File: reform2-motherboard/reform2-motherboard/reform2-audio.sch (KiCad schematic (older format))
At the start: 36 parts, among them J21 Conn_01x04_Male, J7 SJ-43516-SMT, U20 WM8731, U21 MAX9715ETE+

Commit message: reform2: first motherboard fully routed, checks TBD
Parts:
- added J16: LINE_IN, Connector_PinHeader_2.54mm:PinHeader_1x03_P2.54mm_Vertical, symbol Connector:Conn_01x03_Male
- added R112, R66: 220, Resistor_SMD:R_0603_1608Metric, symbol Device:R_Small
- added R114, R121, R150, R151: 33, Resistor_SMD:R_0603_1608Metric, symbol Device:R_Small
- added R152: 0, Resistor_SMD:R_0603_1608Metric, symbol Device:R_Small
- added TP1: T_GAIN, TestPoint:TestPoint_Pad_1.0x1.0mm, symbol Connector:TestPoint
- J21: footprint Connector_PinSocket_2.54mm:PinSocket_1x04_P2.54mm_Vertical -> Connector_PinHeader_2.54mm:PinHeader_1x04_P2.54mm_Vertical
- R138: value 0 -> 33
- R139: value 100 -> 33; Manufacturer Vishay Dale -> (none); Manufacturer_No CRCW0603100RFKEAC -> (none)
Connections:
- net +5V: now also R152.2
- net DAC_BCLK: now also R114.1; no longer U20.3 (BCLK)
- net DAC_DIN: now also R150.1; no longer U20.6 (ADCDAT)
- net DAC_DOUT: now also R121.1; no longer U20.4 (DACDAT)
- net DAC_RXFS: now also R139.1; no longer U20.7 (ADCLRC)
- net DAC_SCL: now also R66.1; no longer R135.2, U20.24 (SCLK)
- net DAC_SDA: now also R112.1; no longer R136.2, U20.23 (SDIN)
- net DAC_TXFS: now also R151.1; no longer U20.5 (DACLRC)
- net GND: now also J16.1 (Pin_1)
- net at U20.19 (RLINEIN): now also J16.2 (Pin_2)
- net at U20.2 (CLKOUT): no longer R139.1
- net at U20.20 (LLINEIN): now also J16.3 (Pin_3)
- net at R139.2: now also U20.7 (ADCLRC)
- net at U21.6 (GAIN): now also TP1.1
- net at U21.8 (~SHDN): now also R152.1
- new net: R135.2, R66.2, U20.24 (SCLK)
- new net: R112.2, R136.2, U20.23 (SDIN)
- new net: R114.2, U20.3 (BCLK)
- new net: R121.2, U20.4 (DACDAT)
- new net: R151.2, U20.5 (DACLRC)
- new net: R150.2, U20.6 (ADCDAT)
- no-connect marks 1 -> 2
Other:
- note removed: "TODO: check MCLK"
- note removed: "TODO: gain & shdn"
- note removed: "TODO: line in header"
- note removed: "TODO: series Rs?"
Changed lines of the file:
@@
 U 1 1 5F0A0C67
 P 3850 5350
-F 0 "R137" V 3750 5200 50  0000 C CNN
+F 0 "R137" V 3950 5350 50  0000 C CNN
 F 1 "10k" V 3750 5350 50  0000 C CNN
 F 2 "Resistor_SMD:R_0603_1608Metric" H 3850 5350 50  0001 C CNN
@@
 	1    0    0    -1
 $EndComp
-$Comp
-L Device:R_Small R139
-U 1 1 5F0ACDC8
-P 5400 5300
-F 0 "R139" V 5300 5150 50  0000 C CNN
-F 1 "100" V 5300 5300 50  0000 C CNN
-F 2 "Resistor_SMD:R_0603_1608Metric" H 5400 5300 50  0001 C CNN
-F 3 "~" H 5400 5300 50  0001 C CNN
-F 4 "Vishay Dale" H 5400 5300 50  0001 C CNN "Manufacturer"
-F 5 "CRCW0603100RFKEAC" H 5400 5300 50  0001 C CNN "Manufacturer_No"
-	1    5400 5300
-	0    -1   -1   0
-$EndComp
-NoConn ~ 5500 5300
+NoConn ~ 5300 5300
 $Comp
 L power:+3V3 #PWR085
@@
 Wire Wire Line
 	4100 5350 4200 5350
-Text GLabel 2250 5150 0    50   BiDi ~ 0
+Text GLabel 1800 5150 0    50   BiDi ~ 0
 DAC_SDA
-Wire Wire Line
-	2250 5150 2750 5150
-Text GLabel 2250 5050 0    50   Input ~ 0
+Text GLabel 1800 5050 0    50   Input ~ 0
 DAC_SCL
-Text GLabel 3700 3950 0    50   Input ~ 0
+Text GLabel 2800 3950 0    50   Input ~ 0
 DAC_TXFS
-Text GLabel 3700 3850 0    50   Input ~ 0
+Text GLabel 2800 3850 0    50   Input ~ 0
 DAC_DOUT
-Wire Wire Line
-	3700 3850 4200 3850
-Text GLabel 3700 4050 0    50   Output ~ 0
+Text GLabel 2800 4050 0    50   Output ~ 0
 DAC_DIN
-Wire Wire Line
-	3700 4050 4200 4050
-Text GLabel 3700 4250 0    50   Input ~ 0
+Text GLabel 2800 4250 0    50   Input ~ 0
 DAC_BCLK
-Wire Wire Line
-	4200 4250 3700 4250
 Text Notes 6300 5800 0    50   ~ 0
 TODO: chokes?
-Wire Wire Line
-	3700 3950 4200 3950
-Text GLabel 3700 4150 0    50   Input ~ 0
+Text GLabel 2800 4150 0    50   Input ~ 0
 DAC_RXFS
-Wire Wire Line
-	3700 4150 4200 4150
 Text GLabel 3700 4750 0    50   Input ~ 0
 DAC_MCLK
@@
 Wire Wire Line
 	6350 4450 6350 4400
-Text Notes 2550 3950 0    50   ~ 0
-TODO: series Rs?
 $Comp
 L Amplifier_Audio:MAX9715ETE+ U21
@@
 F 0 "J21" H 8872 2332 50  0000 R CNN
 F 1 "Conn_01x04_Male" H 8872 2423 50  0000 R CNN
-F 2 "Connector_PinSocket_2.54mm:PinSocket_1x04_P2.54mm_Vertical" H 8900 2450 50  0001 C CNN
+F 2 "Connector_PinHeader_2.54mm:PinHeader_1x04_P2.54mm_Vertical" H 8900 2450 50  0001 C CNN
 F 3 "~" H 8900 2450 50  0001 C CNN
 F 4 "TE" H 8900 2450 50  0001 C CNN "Manufacturer"
@@
 Wire Wire Line
 	5850 3600 5300 3600
-Text Notes 4700 2350 0    50   ~ 0
-TODO: line in header
-Text Notes 6050 2500 0    50   ~ 0
-TODO: gain & shdn
 $Comp
 L Device:C_Small C155
@@
 P 3950 4750
 F 0 "R138" V 3850 4750 50  0000 C CNN
-F 1 "0" V 3950 4750 50  0000 C CNN
+F 1 "33" V 3950 4750 50  0000 C CNN
 F 2 "Resistor_SMD:R_0603_1608Metric" H 3950 4750 50  0001 C CNN
 F 3 "~" H 3950 4750 50  0001 C CNN
@@
 Wire Wire Line
 	3700 4750 3850 4750
-Text Notes 3000 4600 0    50   ~ 0
-TODO: check MCLK
 $Comp
 L Device:R_Small R135
@@
 Wire Wire Line
 	2450 4900 2450 5050
-Wire Wire Line
-	2250 5050 2450 5050
 Connection ~ 2450 5050
 Wire Wire Line
@@
 	0    1    1    0
 $EndComp
+$Comp
+L Device:R_Small R114
+U 1 1 6187A8E2
+P 2900 4250
+F 0 "R114" V 2800 4250 50  0000 C CNN
+F 1 "33" V 2900 4250 50  0000 C CNN
+F 2 "Resistor_SMD:R_0603_1608Metric" H 2900 4250 50  0001 C CNN
+F 3 "~" H 2900 4250 50  0001 C CNN
+	1    2900 4250
+	0    -1   -1   0
+$EndComp
+Wire Wire Line
+	3000 4250 4200 4250
+$Comp
+L Device:R_Small R139
+U 1 1 6187EFD7
+P 3100 4150
+F 0 "R139" V 3000 4150 50  0000 C CNN
+F 1 "33" V 3100 4150 50  0000 C CNN
+F 2 "Resistor_SMD:R_0603_1608Metric" H 3100 4150 50  0001 C CNN
+F 3 "~" H 3100 4150 50  0001 C CNN
+	1    3100 4150
+	0    -1   -1   0
+$EndComp
+Wire Wire Line
+	3000 4150 2800 4150
+Wire Wire Line
+	3200 4150 4200 4150
+$Comp
+L Device:R_Small R150
+U 1 1 6188C0BD
+P 3300 4050
+F 0 "R150" V 3200 4050 50  0000 C CNN
+F 1 "33" V 3300 4050 50  0000 C CNN
+F 2 "Resistor_SMD:R_0603_1608Metric" H 3300 4050 50  0001 C CNN
+F 3 "~" H 3300 4050 50  0001 C CNN
+	1    3300 4050
+	0    -1   -1   0
+$EndComp
+$Comp
+L Device:R_Small R151
+U 1 1 6188C251
+P 3500 3950
+F 0 "R151" V 3400 3950 50  0000 C CNN
+F 1 "33" V 3500 3950 50  0000 C CNN
+F 2 "Resistor_SMD:R_0603_1608Metric" H 3500 3950 50  0001 C CNN
+F 3 "~" H 3500 3950 50  0001 C CNN
+	1    3500 3950
+	0    -1   -1   0
+$EndComp
+$Comp
+L Device:R_Small R121
+U 1 1 6188C4A7
+P 3100 3850
+F 0 "R121" V 3200 3850 50  0000 C CNN
+F 1 "33" V 3100 3850 50  0000 C CNN
+F 2 "Resistor_SMD:R_0603_1608Metric" H 3100 3850 50  0001 C CNN
+F 3 "~" H 3100 3850 50  0001 C CNN
+	1    3100 3850
+	0    -1   -1   0
+$EndComp
+Wire Wire Line
+	3200 3850 4200 3850
+Wire Wire Line
+	3600 3950 4200 3950
+Wire Wire Line
+	3400 4050 4200 4050
+Wire Wire Line
+	3200 4050 2800 4050
+Wire Wire Line
+	2800 3950 3400 3950
+Wire Wire Line
+	3000 3850 2800 3850
+$Comp
+L Device:R_Small R66
+U 1 1 618CAF93
+P 2000 5050
+F 0 "R66" V 2100 5050 50  0000 C CNN
+F 1 "220" V 2000 5050 50  0000 C CNN
+F 2 "Resistor_SMD:R_0603_1608Metric" H 2000 5050 50  0001 C CNN
+F 3 "~" H 2000 5050 50  0001 C CNN
+	1    2000 5050
+	0    -1   -1   0
+$EndComp
+$Comp
+L Device:R_Small R112
+U 1 1 618CB2D9
+P 2000 5150
+F 0 "R112" V 1900 5150 50  0000 C CNN
+F 1 "220" V 2000 5150 50  0000 C CNN
+F 2 "Resistor_SMD:R_0603_1608Metric" H 2000 5150 50  0001 C CNN
+F 3 "~" H 2000 5150 50  0001 C CNN
+	1    2000 5150
+	0    -1   -1   0
+$EndComp
+Wire Wire Line
+	2100 5050 2450 5050
+Wire Wire Line
+	2100 5150 2750 5150
+Wire Wire Line
+	1900 5150 1800 5150
+Wire Wire Line
+	1800 5050 1900 5050
+NoConn ~ 4200 4550
+$Comp
+L Connector:TestPoint TP1
+U 1 1 6191F3C6
+P 6000 2750
+F 0 "TP1" H 5942 2776 50  0000 R CNN
+F 1 "T_GAIN" H 5942 2867 50  0000 R CNN
+F 2 "TestPoint:TestPoint_Pad_1.0x1.0mm" H 6200 2750 50  0001 C CNN
+F 3 "~" H 6200 2750 50  0001 C CNN
+	1    6000 2750
+	-1   0    0    1
+$EndComp
+Wire Wire Line
+	6900 2400 6000 2400
+Wire Wire Line
+	6000 2400 6000 2750
+$Comp
+L Connector:Conn_01x03_Male J16
+U 1 1 61932C31
+P 4950 2000
+F 0 "J16" H 5050 2350 50  0000 C CNN
+F 1 "LINE_IN" H 5050 2250 50  0000 C CNN
+F 2 "Connector_PinHeader_2.54mm:PinHeader_1x03_P2.54mm_Vertical" H 4950 2000 50  0001 C CNN
+F 3 "~" H 4950 2000 50  0001 C CNN
+	1    4950 2000
+	1    0    0    -1
+$EndComp
+Wire Wire Line
+	5300 3200 5600 3200
+Wire Wire Line
+	5600 3200 5600 2000
+Wire Wire Line
+	5600 2000 5150 2000
+Wire Wire Line
+	5300 3000 5500 3000
+Wire Wire Line
+	5500 3000 5500 2100
+Wire Wire Line
+	5500 2100 5150 2100
+$Comp
+L power:GND #PWR041
+U 1 1 6193F11B
+P 5450 1900
+F 0 "#PWR041" H 5450 1650 50  0001 C CNN
+F 1 "GND" V 5455 1772 50  0000 R CNN
+F 2 "" H 5450 1900 50  0001 C CNN
+F 3 "" H 5450 1900 50  0001 C CNN
+	1    5450 1900
+	0    -1   -1   0
+$EndComp
+Wire Wire Line
+	5450 1900 5150 1900
+$Comp
+L Device:R_Small R152
+U 1 1 619BF57F
+P 6750 2500
+F 0 "R152" V 6850 2500 50  0000 C CNN
+F 1 "0" V 6750 2500 50  0000 C CNN
+F 2 "Resistor_SMD:R_0603_1608Metric" H 6750 2500 50  0001 C CNN
+F 3 "~" H 6750 2500 50  0001 C CNN
+	1    6750 2500
+	0    1    1    0
+$EndComp
+Wire Wire Line
+	6850 2500 6900 2500
+$Comp
+L power:+5V #PWR042
+U 1 1 619CBE4D
+P 6450 2500
+F 0 "#PWR042" H 6450 2350 50  0001 C CNN
+F 1 "+5V" V 6465 2628 50  0000 L CNN
+F 2 "" H 6450 2500 50  0001 C CNN
+F 3 "" H 6450 2500 50  0001 C CNN
+	1    6450 2500
+	0    -1   -1   0
+$EndComp
+Wire Wire Line
+	6450 2500 6650 2500
 $EndSCHEMATC

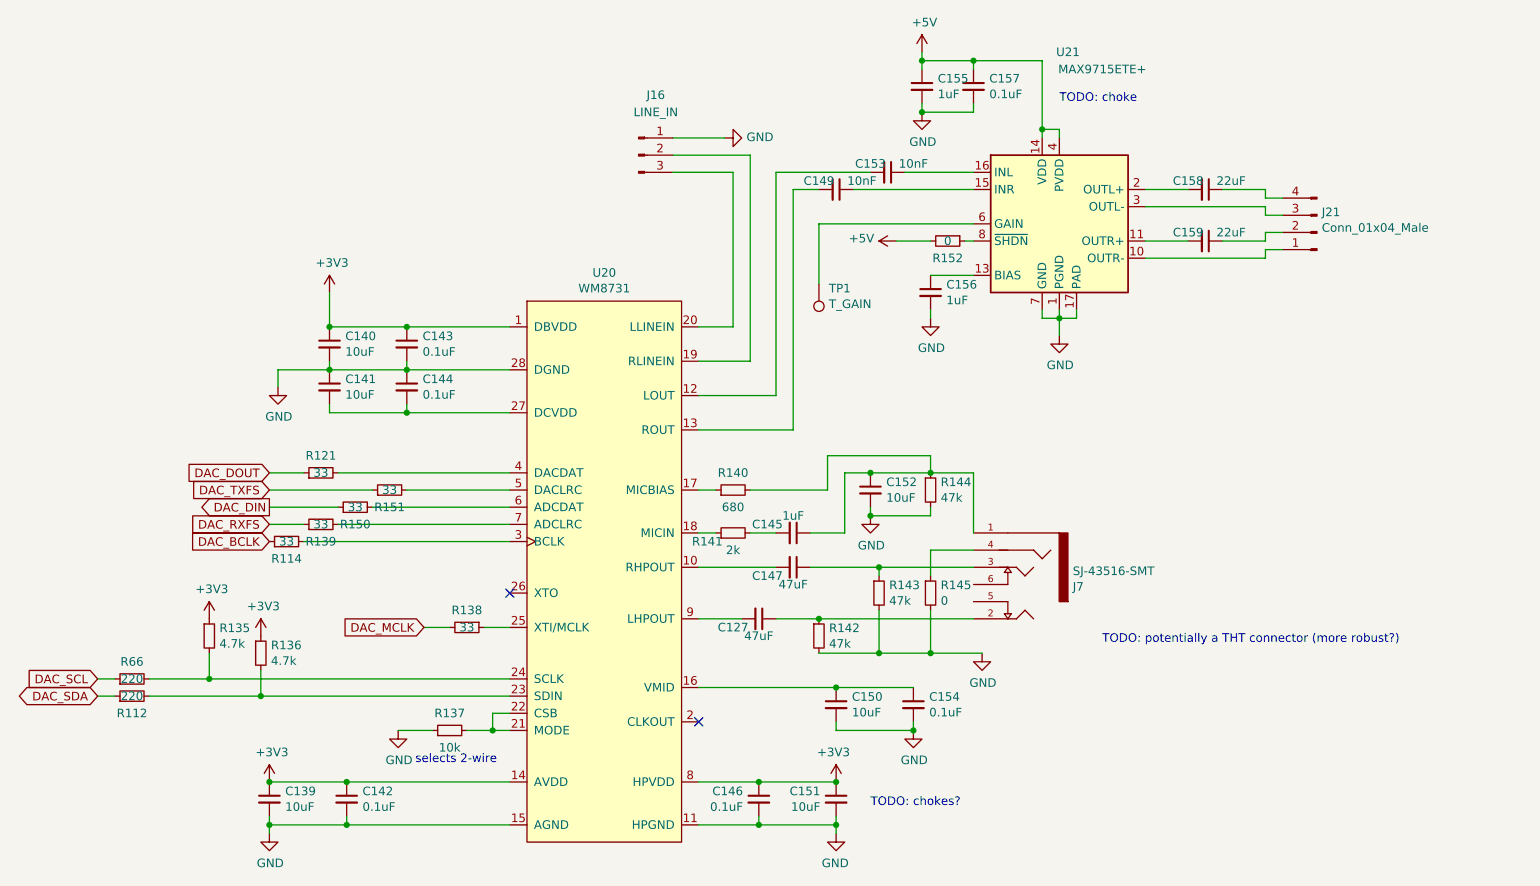
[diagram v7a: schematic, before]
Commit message: reform2 motherboard: pinout and footprint checks completed; ERC checks fixed 100%
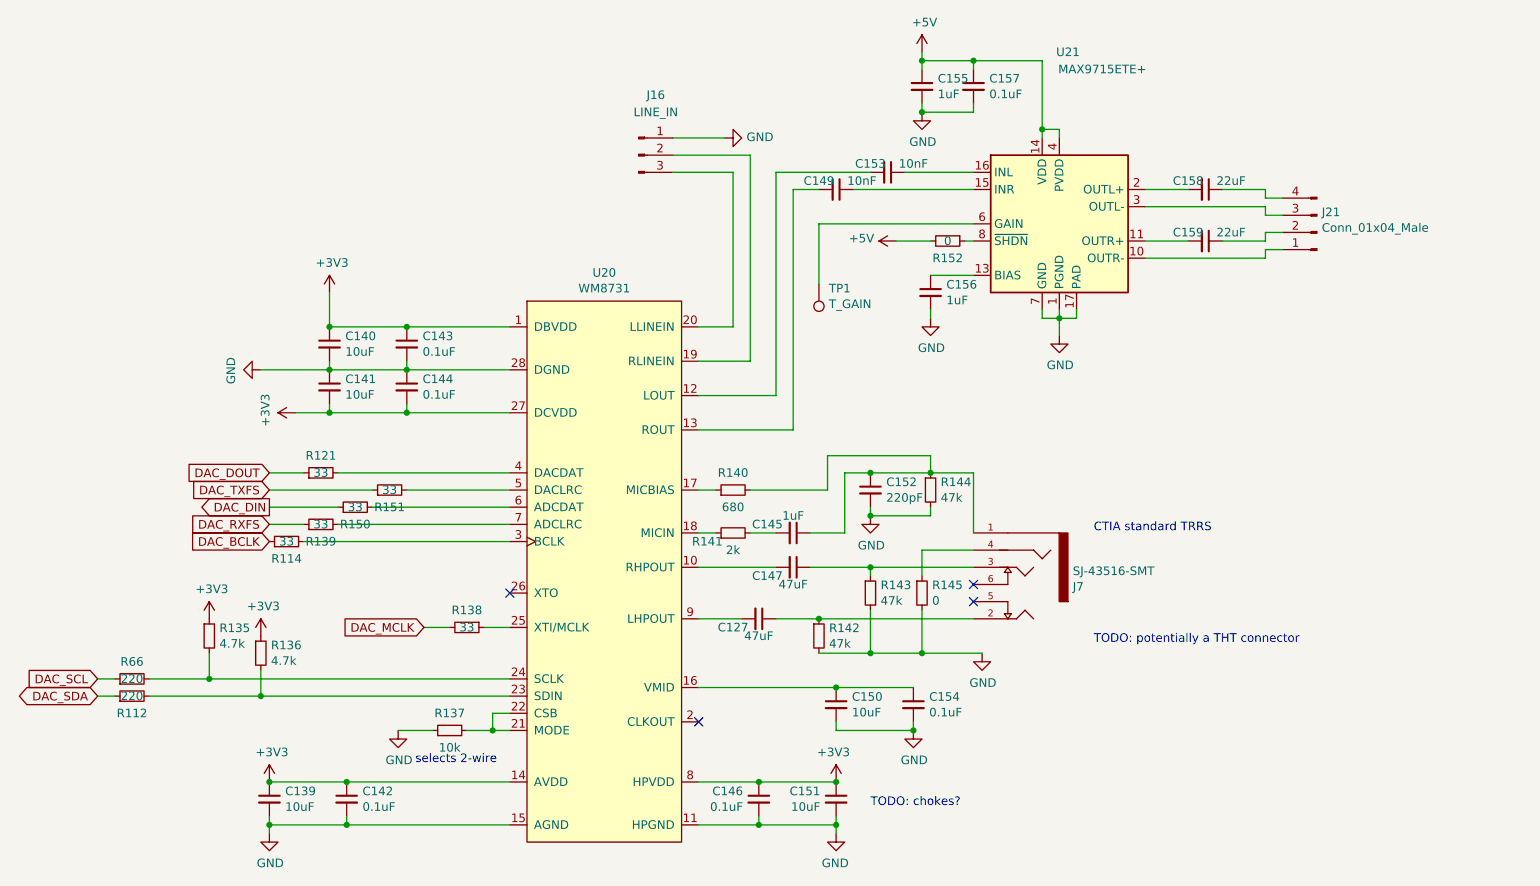
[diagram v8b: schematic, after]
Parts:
- C152: value 10uF -> 220pF
- TP1: footprint TestPoint:TestPoint_Pad_1.0x1.0mm -> TestPoint:TestPoint_Pad_D1.0mm
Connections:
- net +3V3: now also C141.2, C144.2, U20.27 (DCVDD)
- no-connect marks 2 -> 4
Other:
- note added: "CTIA standard TRRS"
- note added: "TODO: potentially a THT connector"
- note removed: "TODO: choke"
- note removed: "TODO: potentially a THT connector (more robust?)"
- moved on the sheet: R143, R145
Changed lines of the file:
@@
 	-1   0    0    -1
 $EndComp
-Text Notes 7650 4850 0    50   ~ 0
-TODO: potentially a THT connector (more robust?)
+Text Notes 7600 4850 0    50   ~ 0
+TODO: potentially a THT connector
 $Comp
 L reform2:WM8731 U20
@@
 L power:GND #PWR087
 U 1 1 5F09C621
-P 2850 3350
-F 0 "#PWR087" H 2850 3100 50  0001 C CNN
-F 1 "GND" H 2855 3177 50  0000 C CNN
-F 2 "" H 2850 3350 50  0001 C CNN
-F 3 "" H 2850 3350 50  0001 C CNN
-	1    2850 3350
-	1    0    0    -1
-$EndComp
-Wire Wire Line
-	2850 3350 2850 3250
-Wire Wire Line
-	2850 3250 3150 3250
+P 2750 3250
+F 0 "#PWR087" H 2750 3000 50  0001 C CNN
+F 1 "GND" H 2755 3077 50  0000 C CNN
+F 2 "" H 2750 3250 50  0001 C CNN
+F 3 "" H 2750 3250 50  0001 C CNN
+	1    2750 3250
+	0    1    1    0
+$EndComp
 Connection ~ 3150 3250
 $Comp
@@
 	5750 4700 6000 4700
 Wire Wire Line
-	5950 4400 6350 4400
+	5950 4400 6300 4400
 Wire Wire Line
 	5750 4400 5300 4400
@@
 L Device:R_Small R143
 U 1 1 5F0DB197
-P 6350 4550
-F 0 "R143" H 6409 4596 50  0000 L CNN
-F 1 "47k" H 6409 4505 50  0000 L CNN
-F 2 "Resistor_SMD:R_0603_1608Metric" H 6350 4550 50  0001 C CNN
-F 3 "~" H 6350 4550 50  0001 C CNN
-F 4 "Vishay Dale" H 6350 4550 50  0001 C CNN "Manufacturer"
-F 5 "CRCW060347K0FKEAC" H 6350 4550 50  0001 C CNN "Manufacturer_No"
-	1    6350 4550
-	1    0    0    -1
-$EndComp
-Connection ~ 6350 4400
-Wire Wire Line
-	6350 4400 6900 4400
+P 6300 4550
+F 0 "R143" H 6359 4596 50  0000 L CNN
+F 1 "47k" H 6359 4505 50  0000 L CNN
+F 2 "Resistor_SMD:R_0603_1608Metric" H 6300 4550 50  0001 C CNN
+F 3 "~" H 6300 4550 50  0001 C CNN
+F 4 "Vishay Dale" H 6300 4550 50  0001 C CNN "Manufacturer"
+F 5 "CRCW060347K0FKEAC" H 6300 4550 50  0001 C CNN "Manufacturer_No"
+	1    6300 4550
+	1    0    0    -1
+$EndComp
+Connection ~ 6300 4400
+Wire Wire Line
+	6300 4400 6900 4400
 $Comp
 L Device:R_Small R142
@@
 $EndComp
 Wire Wire Line
-	6950 4900 6650 4900
-Connection ~ 6350 4900
-Wire Wire Line
-	6350 4900 6000 4900
+	6950 4900 6600 4900
+Connection ~ 6300 4900
+Wire Wire Line
+	6300 4900 6000 4900
 $Comp
 L Device:C_Small C152
@@
 P 6300 3950
 F 0 "C152" H 6392 3996 50  0000 L CNN
-F 1 "10uF" H 6392 3905 50  0000 L CNN
+F 1 "220pF" H 6392 3905 50  0000 L CNN
 F 2 "Capacitor_SMD:C_0603_1608Metric" H 6300 3950 50  0001 C CNN
 F 3 "~" H 6300 3950 50  0001 C CNN
@@
 L Device:R_Small R145
 U 1 1 5F0FC2FD
-P 6650 4550
-F 0 "R145" H 6709 4596 50  0000 L CNN
-F 1 "0" H 6709 4505 50  0000 L CNN
-F 2 "Resistor_SMD:R_0603_1608Metric" H 6650 4550 50  0001 C CNN
-F 3 "~" H 6650 4550 50  0001 C CNN
-F 4 "Vishay Dale" H 6650 4550 50  0001 C CNN "Manufacturer"
-F 5 "CRCW06030000Z0EAC" H 6650 4550 50  0001 C CNN "Manufacturer_No"
-	1    6650 4550
-	1    0    0    -1
-$EndComp
-Wire Wire Line
-	6650 4450 6650 4300
-Wire Wire Line
-	6650 4300 6900 4300
-Wire Wire Line
-	6650 4650 6650 4900
-Connection ~ 6650 4900
-Wire Wire Line
-	6650 4900 6350 4900
+P 6600 4550
+F 0 "R145" H 6659 4596 50  0000 L CNN
+F 1 "0" H 6659 4505 50  0000 L CNN
+F 2 "Resistor_SMD:R_0603_1608Metric" H 6600 4550 50  0001 C CNN
+F 3 "~" H 6600 4550 50  0001 C CNN
+F 4 "Vishay Dale" H 6600 4550 50  0001 C CNN "Manufacturer"
+F 5 "CRCW06030000Z0EAC" H 6600 4550 50  0001 C CNN "Manufacturer_No"
+	1    6600 4550
+	1    0    0    -1
+$EndComp
+Wire Wire Line
+	6600 4450 6600 4300
+Wire Wire Line
+	6600 4300 6900 4300
+Wire Wire Line
+	6600 4650 6600 4900
+Connection ~ 6600 4900
+Wire Wire Line
+	6600 4900 6300 4900
 Wire Wire Line
 	4200 5250 4100 5250
@@
 DAC_MCLK
 Wire Wire Line
-	6350 4650 6350 4900
-Wire Wire Line
-	6350 4450 6350 4400
+	6300 4650 6300 4900
+Wire Wire Line
+	6300 4450 6300 4400
 $Comp
 L Amplifier_Audio:MAX9715ETE+ U21
@@
 Wire Wire Line
 	7300 1850 7300 1900
-Text Notes 7400 1700 0    50   ~ 0
-TODO: choke
 $Comp
 L Device:C_Small C153
@@
 F 0 "TP1" H 5942 2776 50  0000 R CNN
 F 1 "T_GAIN" H 5942 2867 50  0000 R CNN
-F 2 "TestPoint:TestPoint_Pad_1.0x1.0mm" H 6200 2750 50  0001 C CNN
+F 2 "TestPoint:TestPoint_Pad_D1.0mm" H 6200 2750 50  0001 C CNN
 F 3 "~" H 6200 2750 50  0001 C CNN
 	1    6000 2750
@@
 Wire Wire Line
 	6450 2500 6650 2500
+NoConn ~ 6900 4600
+NoConn ~ 6900 4500
+Text Notes 7600 4200 0    50   ~ 0
+CTIA standard TRRS
+Wire Wire Line
+	2750 3250 3150 3250
+$Comp
+L power:+3V3 #PWR0222
+U 1 1 645B5EF6
+P 2950 3500
+F 0 "#PWR0222" H 2950 3350 50  0001 C CNN
+F 1 "+3V3" H 2965 3673 50  0000 C CNN
+F 2 "" H 2950 3500 50  0001 C CNN
+F 3 "" H 2950 3500 50  0001 C CNN
+	1    2950 3500
+	0    -1   -1   0
+$EndComp
+Wire Wire Line
+	2950 3500 3150 3500
+Connection ~ 3150 3500
 $EndSCHEMATC
